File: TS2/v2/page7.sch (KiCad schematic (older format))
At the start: 9 parts, among them P1 FTDI (TERMINAL), P2 FTDI (HOST), U28 74LS04, U29 6850, U30 6850, U31 MC14411, U5 74LS04, Y1 1.842MHz

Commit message: Add jumpers for wait states, add some more text.
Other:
- note added: "1200"
- note added: "2400"
- note added: "300"
- note added: "4800"
- note added: "600"
- note added: "9600"
- note added: "Select baud rate"
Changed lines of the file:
@@
 Connection ~ 6350 1700
 $Comp
-L GND #PWR079
+L GND #PWR080
 U 1 1 57C6835F
 P 7250 2050
-F 0 "#PWR079" H 7250 1800 50  0001 C CNN
+F 0 "#PWR080" H 7250 1800 50  0001 C CNN
 F 1 "GND" H 7250 1900 50  0000 C CNN
 F 2 "" H 7250 2050 50  0000 C CNN
@@
 $EndComp
 $Comp
-L VCC #PWR080
+L VCC #PWR081
 U 1 1 57C6838D
 P 7250 1150
-F 0 "#PWR080" H 7250 1000 50  0001 C CNN
+F 0 "#PWR081" H 7250 1000 50  0001 C CNN
 F 1 "VCC" H 7250 1300 50  0000 C CNN
 F 2 "" H 7250 1150 50  0000 C CNN
@@
 $EndComp
 $Comp
-L GND #PWR081
+L GND #PWR082
 U 1 1 57C688B5
 P 6450 1450
-F 0 "#PWR081" H 6450 1200 50  0001 C CNN
+F 0 "#PWR082" H 6450 1200 50  0001 C CNN
 F 1 "GND" H 6450 1300 50  0000 C CNN
 F 2 "" H 6450 1450 50  0000 C CNN
@@
 $EndComp
 $Comp
-L VCC #PWR082
+L VCC #PWR083
 U 1 1 57C688E3
 P 6450 1250
-F 0 "#PWR082" H 6450 1100 50  0001 C CNN
+F 0 "#PWR083" H 6450 1100 50  0001 C CNN
 F 1 "VCC" H 6450 1400 50  0000 C CNN
 F 2 "" H 6450 1250 50  0000 C CNN
@@
 	3100 3000 2050 3000
 $Comp
-L VCC #PWR083
+L VCC #PWR084
 U 1 1 57C7A398
 P 3800 1650
-F 0 "#PWR083" H 3800 1500 50  0001 C CNN
+F 0 "#PWR084" H 3800 1500 50  0001 C CNN
 F 1 "VCC" H 3800 1800 50  0000 C CNN
 F 2 "" H 3800 1650 50  0000 C CNN
@@
 $EndComp
 $Comp
-L GND #PWR084
+L GND #PWR085
 U 1 1 57C7A4BC
 P 3800 3550
-F 0 "#PWR084" H 3800 3300 50  0001 C CNN
+F 0 "#PWR085" H 3800 3300 50  0001 C CNN
 F 1 "GND" H 3800 3400 50  0000 C CNN
 F 2 "" H 3800 3550 50  0000 C CNN
@@
 $EndComp
 $Comp
-L VCC #PWR085
+L VCC #PWR086
 U 1 1 57C7A5E0
 P 3800 4500
-F 0 "#PWR085" H 3800 4350 50  0001 C CNN
+F 0 "#PWR086" H 3800 4350 50  0001 C CNN
 F 1 "VCC" H 3800 4650 50  0000 C CNN
 F 2 "" H 3800 4500 50  0000 C CNN
@@
 $EndComp
 $Comp
-L GND #PWR086
+L GND #PWR087
 U 1 1 57C7A616
 P 3800 6400
-F 0 "#PWR086" H 3800 6150 50  0001 C CNN
+F 0 "#PWR087" H 3800 6150 50  0001 C CNN
 F 1 "GND" H 3800 6250 50  0000 C CNN
 F 2 "" H 3800 6400 50  0000 C CNN
@@
 	8600 2600 8450 2600
 $Comp
-L GND #PWR087
+L GND #PWR088
 U 1 1 57CB2088
 P 8450 2600
-F 0 "#PWR087" H 8450 2350 50  0001 C CNN
+F 0 "#PWR088" H 8450 2350 50  0001 C CNN
 F 1 "GND" H 8450 2450 50  0000 C CNN
 F 2 "" H 8450 2600 50  0000 C CNN
@@
 	8600 2800 8450 2800
 $Comp
-L VCC #PWR088
+L VCC #PWR089
 U 1 1 57CB20FE
 P 8450 2800
-F 0 "#PWR088" H 8450 2650 50  0001 C CNN
+F 0 "#PWR089" H 8450 2650 50  0001 C CNN
 F 1 "VCC" H 8450 2950 50  0000 C CNN
 F 2 "" H 8450 2800 50  0000 C CNN
@@
 	5200 2400 4500 2400
 $Comp
-L GND #PWR089
+L GND #PWR090
 U 1 1 57CB2D6B
 P 4500 3000
-F 0 "#PWR089" H 4500 2750 50  0001 C CNN
+F 0 "#PWR090" H 4500 2750 50  0001 C CNN
 F 1 "GND" H 4500 2850 50  0000 C CNN
 F 2 "" H 4500 3000 50  0000 C CNN
@@
 $EndComp
 $Comp
-L GND #PWR090
+L GND #PWR091
 U 1 1 57CB394C
 P 8450 5450
-F 0 "#PWR090" H 8450 5200 50  0001 C CNN
+F 0 "#PWR091" H 8450 5200 50  0001 C CNN
 F 1 "GND" H 8450 5300 50  0000 C CNN
 F 2 "" H 8450 5450 50  0000 C CNN
@@
 	8600 5650 8450 5650
 $Comp
-L VCC #PWR091
+L VCC #PWR092
 U 1 1 57CB3ACF
 P 8450 5650
-F 0 "#PWR091" H 8450 5500 50  0001 C CNN
+F 0 "#PWR092" H 8450 5500 50  0001 C CNN
 F 1 "VCC" H 8450 5800 50  0000 C CNN
 F 2 "" H 8450 5650 50  0000 C CNN
@@
 $EndComp
 $Comp
-L GND #PWR092
+L GND #PWR093
 U 1 1 57CB4274
 P 4500 5850
-F 0 "#PWR092" H 4500 5600 50  0001 C CNN
+F 0 "#PWR093" H 4500 5600 50  0001 C CNN
 F 1 "GND" H 4500 5700 50  0000 C CNN
 F 2 "" H 4500 5850 50  0000 C CNN
@@
 Wire Wire Line
 	4800 5950 4500 5950
+Text Notes 8350 1300 0    60   ~ 0
+9600
+Text Notes 8350 1400 0    60   ~ 0
+4800
+Text Notes 8350 1500 0    60   ~ 0
+2400
+Text Notes 8350 1600 0    60   ~ 0
+1200
+Text Notes 8350 1700 0    60   ~ 0
+600
+Text Notes 8350 1800 0    60   ~ 0
+300
+Text Notes 8750 1550 0    60   ~ 0
+Select baud rate
 $EndSCHEMATC

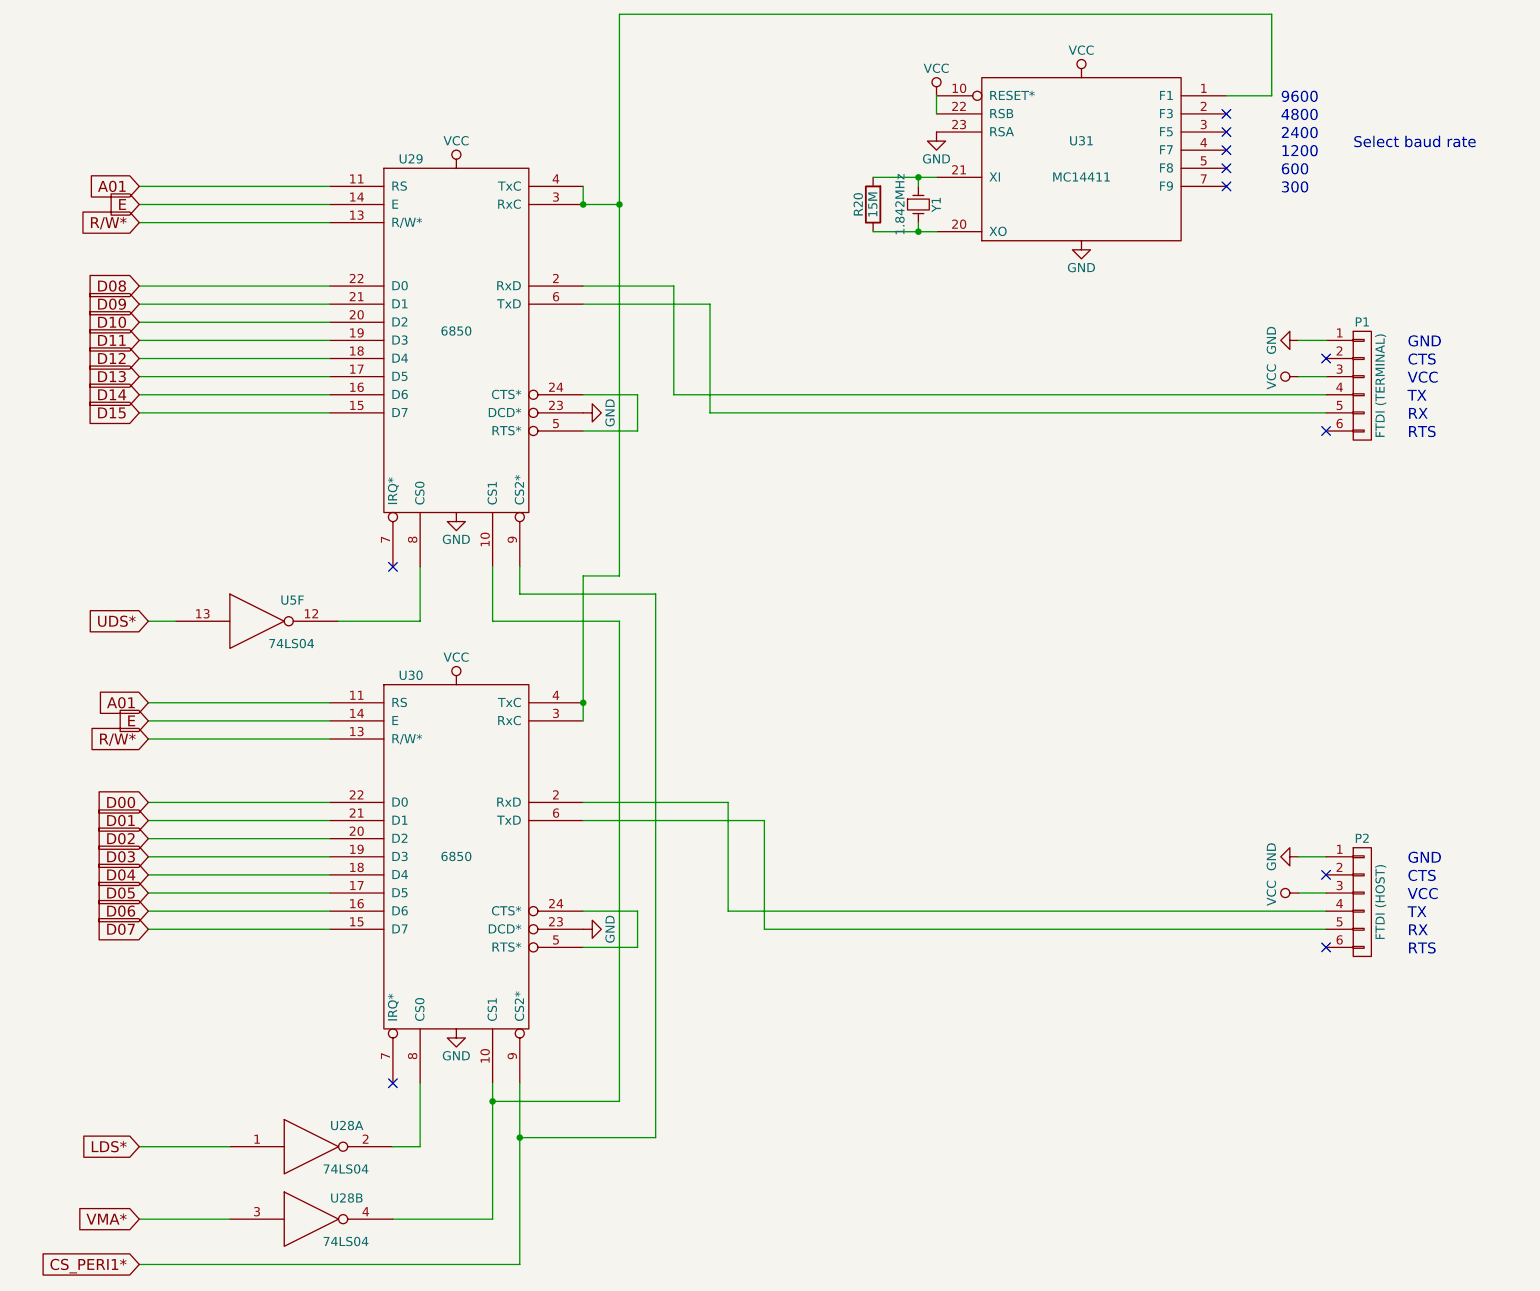
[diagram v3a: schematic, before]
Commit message: Remove two duplicated pullup resistors. Route some signals better.
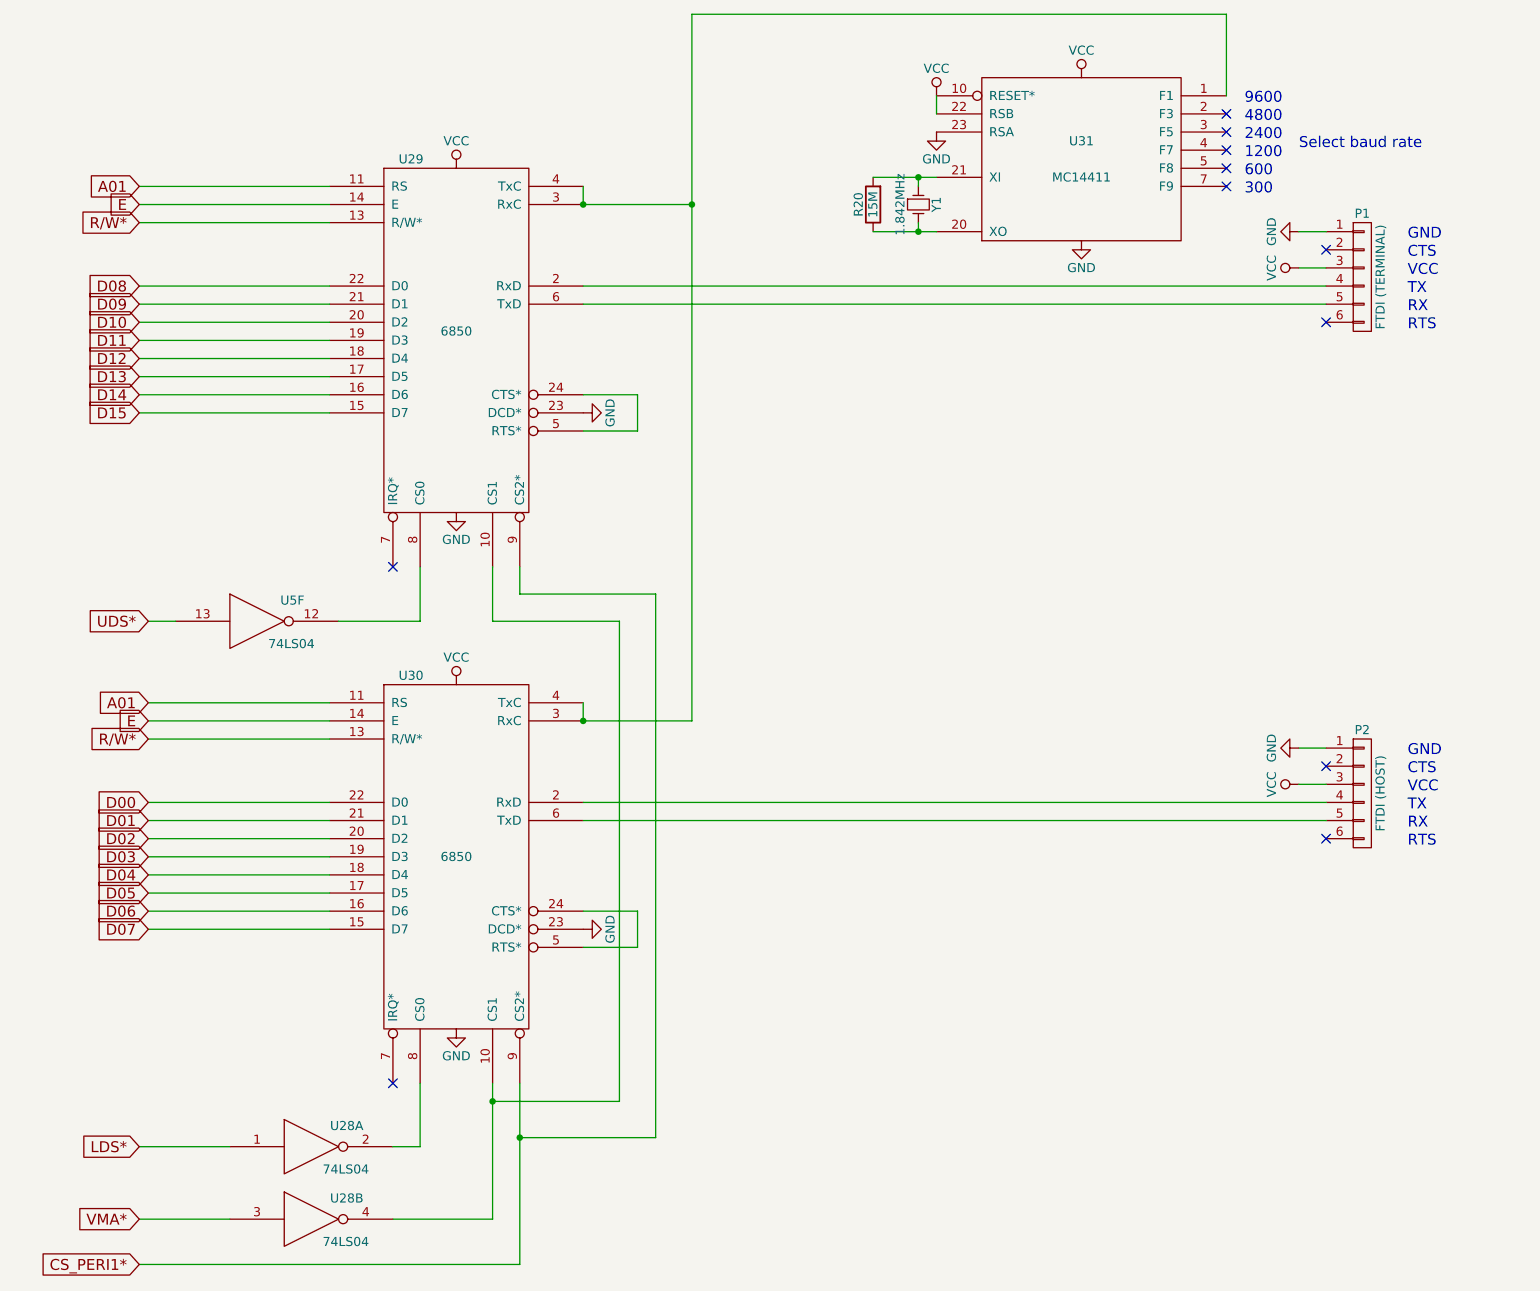
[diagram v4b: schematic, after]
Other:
- moved on the sheet: P1, P2

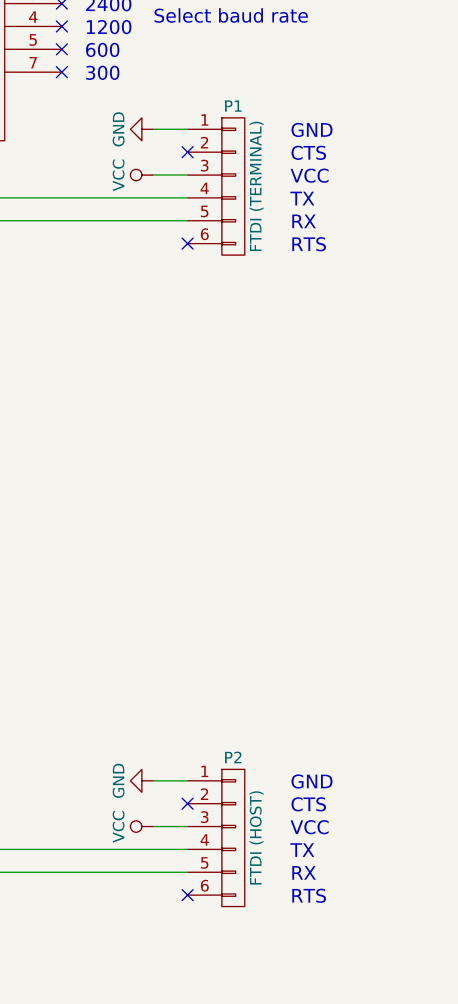
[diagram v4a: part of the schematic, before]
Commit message: Label RAM and ROM chips with address ranges.
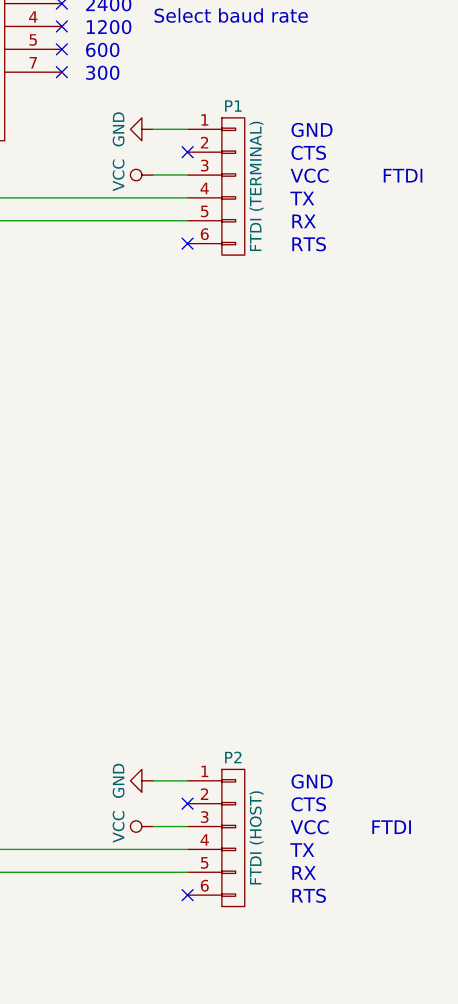
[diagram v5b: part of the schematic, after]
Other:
- note added: "FTDI"
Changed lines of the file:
@@
 Wire Wire Line
 	8050 800  5100 800
+Text Notes 9450 2250 0    60   ~ 0
+FTDI
+Text Notes 9400 5100 0    60   ~ 0
+FTDI
 $EndSCHEMATC

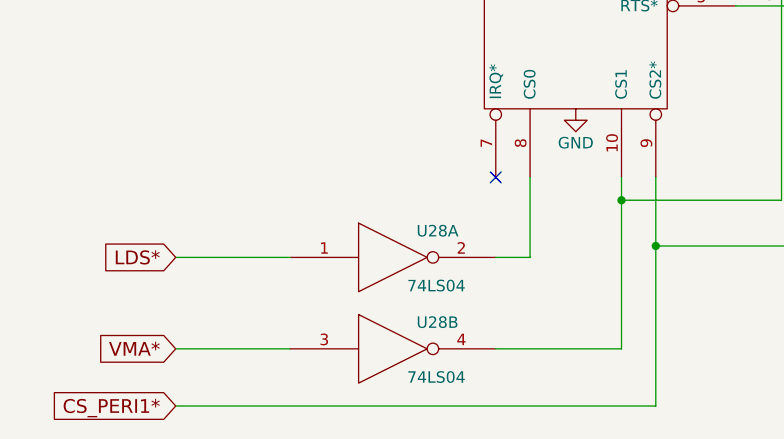
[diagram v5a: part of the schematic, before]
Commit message: ELiminated one chip (U28) by using other unused gates. Added unused gates to schematic.
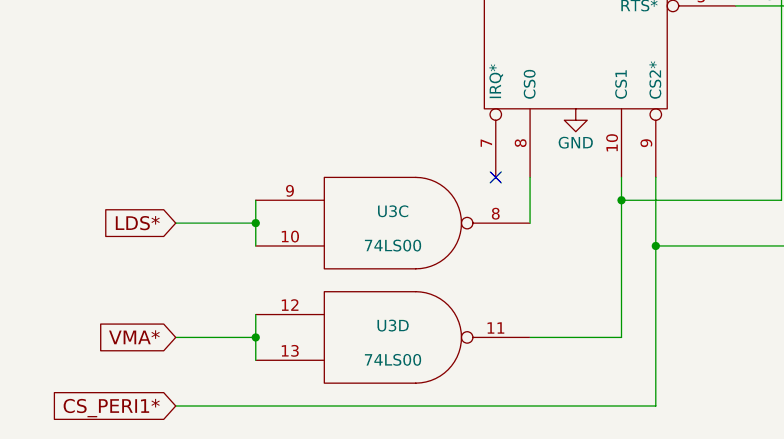
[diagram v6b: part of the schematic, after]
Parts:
- removed U28: 74LS04, symbol 74LS04
- added U3: 74LS00, symbol 74LS00
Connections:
- net GND: now also U3.7 (GND), U3.7 (GND)
- net LDS*: now also U3.10, U3.9
- net VCC: now also U3.14 (VCC), U3.14 (VCC)
- net VMA*: now also U3.12, U3.13
- net at U29.10 (CS1), U30.10 (CS1): now also U3.11
- net at U30.8 (CS0): now also U3.8
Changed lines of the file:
@@
 $EndComp
 $Comp
-L GND #PWR080
+L GND #PWR087
 U 1 1 57C6835F
 P 7250 2050
-F 0 "#PWR080" H 7250 1800 50  0001 C CNN
+F 0 "#PWR087" H 7250 1800 50  0001 C CNN
 F 1 "GND" H 7250 1900 50  0000 C CNN
 F 2 "" H 7250 2050 50  0000 C CNN
@@
 $EndComp
 $Comp
-L VCC #PWR081
+L VCC #PWR088
 U 1 1 57C6838D
 P 7250 1150
-F 0 "#PWR081" H 7250 1000 50  0001 C CNN
+F 0 "#PWR088" H 7250 1000 50  0001 C CNN
 F 1 "VCC" H 7250 1300 50  0000 C CNN
 F 2 "" H 7250 1150 50  0000 C CNN
@@
 $EndComp
 $Comp
-L GND #PWR082
+L GND #PWR089
 U 1 1 57C688B5
 P 6450 1450
-F 0 "#PWR082" H 6450 1200 50  0001 C CNN
+F 0 "#PWR089" H 6450 1200 50  0001 C CNN
 F 1 "GND" H 6450 1300 50  0000 C CNN
 F 2 "" H 6450 1450 50  0000 C CNN
@@
 $EndComp
 $Comp
-L VCC #PWR083
+L VCC #PWR090
 U 1 1 57C688E3
 P 6450 1250
-F 0 "#PWR083" H 6450 1100 50  0001 C CNN
+F 0 "#PWR090" H 6450 1100 50  0001 C CNN
 F 1 "VCC" H 6450 1400 50  0000 C CNN
 F 2 "" H 6450 1250 50  0000 C CNN
@@
 D08
 $Comp
-L 74LS04 U28
-U 1 1 57C69545
-P 3000 7050
-F 0 "U28" H 3195 7165 50  0000 C CNN
-F 1 "74LS04" H 3190 6925 50  0000 C CNN
-F 2 "" H 3000 7050 50  0000 C CNN
-F 3 "" H 3000 7050 50  0000 C CNN
-	1    3000 7050
-	1    0    0    -1
-$EndComp
-$Comp
-L 74LS04 U28
-U 2 1 57C695DB
-P 3000 7450
-F 0 "U28" H 3195 7565 50  0000 C CNN
-F 1 "74LS04" H 3190 7325 50  0000 C CNN
-F 2 "" H 3000 7450 50  0000 C CNN
-F 3 "" H 3000 7450 50  0000 C CNN
-	2    3000 7450
-	1    0    0    -1
-$EndComp
-$Comp
 L 74LS04 U5
 U 6 1 57C69631
@@
 NoConn ~ 3450 3850
 NoConn ~ 3450 6700
-Text GLabel 2050 7050 0    60   Input ~ 0
+Text GLabel 2050 6900 0    60   Input ~ 0
 LDS*
-Text GLabel 2050 7450 0    60   Input ~ 0
+Text GLabel 2050 7400 0    60   Input ~ 0
 VMA*
 Text GLabel 2050 7700 0    60   Input ~ 0
@@
 D15
 $Comp
-L VCC #PWR084
+L VCC #PWR091
 U 1 1 57C7A398
 P 3800 1650
-F 0 "#PWR084" H 3800 1500 50  0001 C CNN
+F 0 "#PWR091" H 3800 1500 50  0001 C CNN
 F 1 "VCC" H 3800 1800 50  0000 C CNN
 F 2 "" H 3800 1650 50  0000 C CNN
@@
 $EndComp
 $Comp
-L GND #PWR085
+L GND #PWR092
 U 1 1 57C7A4BC
 P 3800 3550
-F 0 "#PWR085" H 3800 3300 50  0001 C CNN
+F 0 "#PWR092" H 3800 3300 50  0001 C CNN
 F 1 "GND" H 3800 3400 50  0000 C CNN
 F 2 "" H 3800 3550 50  0000 C CNN
@@
 $EndComp
 $Comp
-L VCC #PWR086
+L VCC #PWR093
 U 1 1 57C7A5E0
 P 3800 4500
-F 0 "#PWR086" H 3800 4350 50  0001 C CNN
+F 0 "#PWR093" H 3800 4350 50  0001 C CNN
 F 1 "VCC" H 3800 4650 50  0000 C CNN
 F 2 "" H 3800 4500 50  0000 C CNN
@@
 $EndComp
 $Comp
-L GND #PWR087
+L GND #PWR094
 U 1 1 57C7A616
 P 3800 6400
-F 0 "#PWR087" H 3800 6150 50  0001 C CNN
+F 0 "#PWR094" H 3800 6150 50  0001 C CNN
 F 1 "GND" H 3800 6250 50  0000 C CNN
 F 2 "" H 3800 6400 50  0000 C CNN
@@
 $EndComp
 $Comp
-L GND #PWR088
+L GND #PWR095
 U 1 1 57CB2088
 P 8450 2000
-F 0 "#PWR088" H 8450 1750 50  0001 C CNN
+F 0 "#PWR095" H 8450 1750 50  0001 C CNN
 F 1 "GND" H 8450 1850 50  0000 C CNN
 F 2 "" H 8450 2000 50  0000 C CNN
@@
 $EndComp
 $Comp
-L VCC #PWR089
+L VCC #PWR096
 U 1 1 57CB20FE
 P 8450 2200
-F 0 "#PWR089" H 8450 2050 50  0001 C CNN
+F 0 "#PWR096" H 8450 2050 50  0001 C CNN
 F 1 "VCC" H 8450 2350 50  0000 C CNN
 F 2 "" H 8450 2200 50  0000 C CNN
@@
 $EndComp
 $Comp
-L GND #PWR090
+L GND #PWR097
 U 1 1 57CB2D6B
 P 4500 3000
-F 0 "#PWR090" H 4500 2750 50  0001 C CNN
+F 0 "#PWR097" H 4500 2750 50  0001 C CNN
 F 1 "GND" H 4500 2850 50  0000 C CNN
 F 2 "" H 4500 3000 50  0000 C CNN
@@
 $EndComp
 $Comp
-L GND #PWR091
+L GND #PWR098
 U 1 1 57CB394C
 P 8450 4850
-F 0 "#PWR091" H 8450 4600 50  0001 C CNN
+F 0 "#PWR098" H 8450 4600 50  0001 C CNN
 F 1 "GND" H 8450 4700 50  0000 C CNN
 F 2 "" H 8450 4850 50  0000 C CNN
@@
 $EndComp
 $Comp
-L VCC #PWR092
+L VCC #PWR099
 U 1 1 57CB3ACF
 P 8450 5050
-F 0 "#PWR092" H 8450 4900 50  0001 C CNN
+F 0 "#PWR099" H 8450 4900 50  0001 C CNN
 F 1 "VCC" H 8450 5200 50  0000 C CNN
 F 2 "" H 8450 5050 50  0000 C CNN
@@
 $EndComp
 $Comp
-L GND #PWR093
+L GND #PWR0100
 U 1 1 57CB4274
 P 4500 5850
-F 0 "#PWR093" H 4500 5600 50  0001 C CNN
+F 0 "#PWR0100" H 4500 5600 50  0001 C CNN
 F 1 "GND" H 4500 5700 50  0000 C CNN
 F 2 "" H 4500 5850 50  0000 C CNN
@@
 	4500 1850 4500 1750
 Wire Wire Line
-	2050 7050 2550 7050
-Wire Wire Line
-	3450 7050 3600 7050
-Wire Wire Line
-	3600 7050 3600 6700
-Wire Wire Line
-	2050 7450 2550 7450
-Wire Wire Line
-	4000 7450 3450 7450
-Wire Wire Line
-	4000 6700 4000 7450
-Wire Wire Line
 	4150 6700 4150 7700
 Wire Wire Line
@@
 Text Notes 9400 5100 0    60   ~ 0
 FTDI
+$Comp
+L 74LS00 U3
+U 3 1 5842F0A3
+P 3000 6900
+F 0 "U3" H 3000 6950 50  0000 C CNN
+F 1 "74LS00" H 3000 6800 50  0000 C CNN
+F 2 "" H 3000 6900 50  0000 C CNN
+F 3 "" H 3000 6900 50  0000 C CNN
+	3    3000 6900
+	1    0    0    -1
+$EndComp
+$Comp
+L 74LS00 U3
+U 4 1 5842F155
+P 3000 7400
+F 0 "U3" H 3000 7450 50  0000 C CNN
+F 1 "74LS00" H 3000 7300 50  0000 C CNN
+F 2 "" H 3000 7400 50  0000 C CNN
+F 3 "" H 3000 7400 50  0000 C CNN
+	4    3000 7400
+	1    0    0    -1
+$EndComp
+Wire Wire Line
+	3600 6700 3600 6900
+Wire Wire Line
+	2400 6800 2400 7000
+Wire Wire Line
+	2400 6900 2050 6900
+Connection ~ 2400 6900
+Wire Wire Line
+	4000 6700 4000 7400
+Wire Wire Line
+	4000 7400 3600 7400
+Wire Wire Line
+	2400 7300 2400 7500
+Wire Wire Line
+	2400 7400 2050 7400
+Connection ~ 2400 7400
 $EndSCHEMATC
